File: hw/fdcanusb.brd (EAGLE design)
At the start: 45 x 32 mm, 37 parts, among them J3 JST-ZH6SMT_VERT, M1 MOUNT, M2 MOUNT, M3 MOUNT, M4 MOUNT, U1 MF-REG-SOT235-3.3V-300mA, U2 USBLC6-2SC6, U3 TCAN334GSOT23, U4 TLP3317, U5 STM32G474CEU6

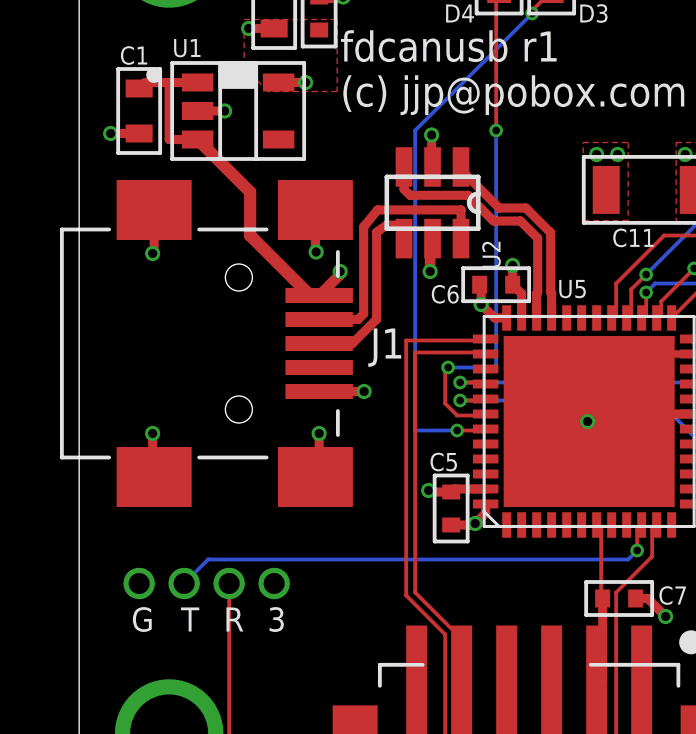
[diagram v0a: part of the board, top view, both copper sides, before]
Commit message: Switch to actually using a micro USB connector
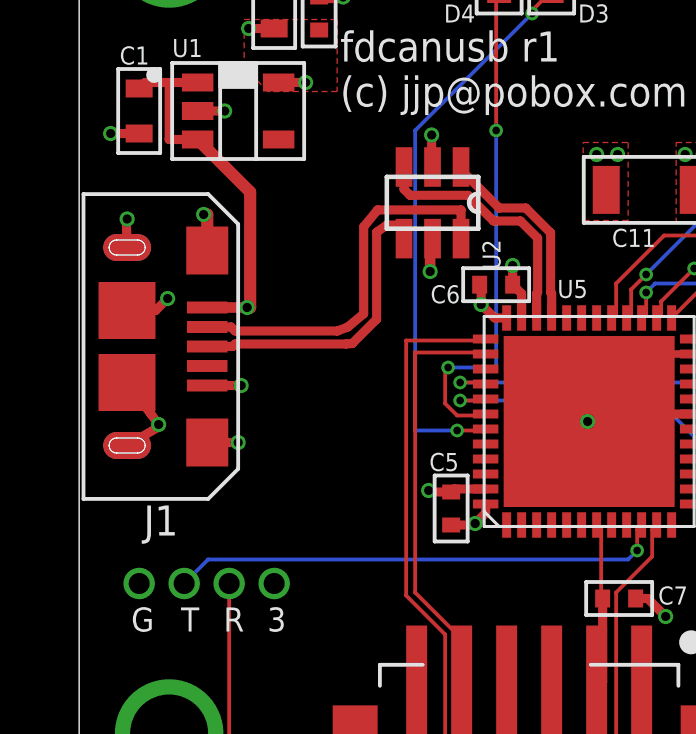
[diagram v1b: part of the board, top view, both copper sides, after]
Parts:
- J1: value (none) -> MF-CON-MICROUSB-RIGHT; device mfconnectors:MINIUSB-RIGHT -> mfconnectors:MICROUSB-RIGHT
- moved J1 5.00 mm to (3.00, 15.9)
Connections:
- net GND: now also J1.S5, J1.S6
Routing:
- net USB_D_N: track 8.93 -> 12.8 mm
- net USB_D_P: track 6.59 -> 10.4 mm
- net VBUS: track 17.2 -> 20.0 mm
- net GND: track 35.9 -> 37.6 mm, vias 25 -> 26
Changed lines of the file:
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@@
 <attribute name="POPULATE" value="0" x="3" y="29" size="1.778" layer="27" display="off"/>
 </element>
-<element name="J1" library="mfconnectors" package="MINIUSB-RIGHT" value="" x="8" y="16" smashed="yes" rot="R270">
-<attribute name="MPN" value="MF-CON-MICROUSB-RIGHT" x="-26.29" y="-20.83" size="1.778" layer="27" rot="R270" display="off"/>
-<attribute name="POPULATE" value="1" x="-26.29" y="-20.83" size="1.778" layer="27" rot="R270" display="off"/>
-<attribute name="HUOSEPART" value="YES" x="-26.29" y="-20.83" size="1.778" layer="27" rot="R270" display="off"/>
-<attribute name="URL" value="http://www.4uconnector.com/online/object/4udrawing/20236.pdf" x="-26.29" y="-20.83" size="1.778" layer="27" rot="R270" display="off"/>
-<attribute name="NAME" x="9.7" y="15.5" size="1" layer="25" font="vector" ratio="10"/>
+<element name="J1" library="mfconnectors" package="MICROUSB-RIGHT" value="MF-CON-MICROUSB-RIGHT" x="3" y="15.9" smashed="yes" rot="R270">
+<attribute name="MPN" value="MF-CON-MICROUSB-RIGHT" x="-31.29" y="-20.93" size="1.778" layer="27" rot="R270" display="off"/>
+<attribute name="POPULATE" value="1" x="-31.29" y="-20.93" size="1.778" layer="27" rot="R270" display="off"/>
+<attribute name="URL" value="https://factory.macrofab.com/part/MF-CON-MICROUSB-RIGHT" x="-31.29" y="-20.93" size="1.778" layer="27" rot="R270" display="off"/>
+<attribute name="NAME" x="3.3" y="10.6" size="1" layer="25" font="vector" ratio="10" rot="R180"/>
+<attribute name="HOUSEPART" value="YES" x="3" y="15.9" size="1.778" layer="27" rot="R270" display="off"/>
+<attribute name="VALUE" value="MF-CON-MICROUSB-RIGHT" x="3" y="15.9" size="1.778" layer="27" rot="R270" display="off"/>
 </element>
 <element name="U1" library="mficpower" package="SOT-23-5" value="MF-REG-SOT235-3.3V-300mA" x="5.3" y="23.75" smashed="yes">
@@
 <via x="11.65" y="11.1" extent="1-16" drill="0.3048"/>
 <via x="14.45" y="18.6" extent="1-16" drill="0.3048"/>
-<via x="2.45" y="13" extent="1-16" drill="0.3048"/>
-<via x="2.45" y="19" extent="1-16" drill="0.3048"/>
-<via x="7.9" y="19.05" extent="1-16" drill="0.3048"/>
-<via x="8" y="13" extent="1-16" drill="0.3048"/>
+<via x="2.65" y="13.3" extent="1-16" drill="0.3048"/>
+<via x="2.95" y="17.5" extent="1-16" drill="0.3048"/>
+<via x="1.6" y="20.15" extent="1-16" drill="0.3048"/>
+<via x="5.3" y="12.7" extent="1-16" drill="0.3048"/>
 <via x="11.75" y="22.95" extent="1-16" drill="0.3048"/>
-<via x="9.5" y="14.4" extent="1-16" drill="0.3048"/>
-<wire x1="8" y1="14.4" x2="9.5" y2="14.4" width="0.3048" layer="1"/>
-<wire x1="8" y1="13" x2="8" y2="11.675" width="0.3048" layer="1"/>
-<wire x1="8" y1="11.675" x2="7.875" y2="11.55" width="0.3048" layer="1"/>
-<wire x1="2.45" y1="13" x2="2.45" y2="11.6" width="0.3048" layer="1"/>
-<wire x1="2.45" y1="11.6" x2="2.5" y2="11.55" width="0.3048" layer="1"/>
-<wire x1="2.5" y1="20.45" x2="2.5" y2="19.05" width="0.3048" layer="1"/>
-<wire x1="2.5" y1="19.05" x2="2.45" y2="19" width="0.3048" layer="1"/>
-<wire x1="7.875" y1="20.45" x2="7.875" y2="19.075" width="0.3048" layer="1"/>
-<wire x1="7.875" y1="19.075" x2="7.9" y2="19.05" width="0.3048" layer="1"/>
+<via x="5.4" y="14.6" extent="1-16" drill="0.3048"/>
+<wire x1="4.27" y1="14.6" x2="5.4" y2="14.6" width="0.3048" layer="1"/>
+<wire x1="1.6" y1="19.2" x2="1.575" y2="19.975" width="0.3048" layer="1"/>
+<wire x1="1.575" y1="19.975" x2="1.6" y2="20.15" width="0.3048" layer="1"/>
 <wire x1="2" y1="23" x2="1.05" y2="23" width="0.3048" layer="1"/>
 <wire x1="3.95" y1="23.75" x2="4.85" y2="23.75" width="0.3048" layer="1"/>
@@
 <wire x1="19.25" y1="15.65" x2="17" y2="13.4" width="0.254" layer="1" curve="90"/>
 <wire x1="17" y1="13.4" x2="16.95" y2="13.4" width="0.127" layer="1"/>
+<contactref element="J1" pad="S5"/>
+<contactref element="J1" pad="S6"/>
+<via x="4.15" y="20.3" extent="1-16" drill="0.3048"/>
+<wire x1="2.95" y1="17.5" x2="2.55" y2="17.1" width="0.3048" layer="1"/>
+<wire x1="2.55" y1="17.1" x2="1.595" y2="17.1" width="0.3048" layer="1"/>
+<wire x1="2.65" y1="13.3" x2="2.7" y2="13.25" width="0.3048" layer="1"/>
+<wire x1="2.7" y1="13.25" x2="1.6" y2="12.6" width="0.3048" layer="1"/>
+<wire x1="2.65" y1="13.3" x2="2.395" y2="13.645" width="0.3048" layer="1"/>
+<wire x1="2.395" y1="13.645" x2="1.595" y2="14.7" width="0.3048" layer="1"/>
+<wire x1="5.3" y1="12.7" x2="4.27" y2="12.7" width="0.3048" layer="1"/>
+<wire x1="4.27" y1="19.1" x2="4.27" y2="20.3" width="0.4064" layer="1"/>
+<wire x1="4.27" y1="20.3" x2="4.15" y2="20.3" width="0.4064" layer="1"/>
 </signal>
 <signal name="VBUS">
@@
 <wire x1="3.95" y1="22.8" x2="3" y2="22.8" width="0.3048" layer="1"/>
 <wire x1="3" y1="22.8" x2="3" y2="24.7" width="0.3048" layer="1"/>
-<wire x1="8" y1="17.6" x2="7.7" y2="17.6" width="0.4064" layer="1"/>
-<wire x1="7.7" y1="17.6" x2="5.7" y2="19.6" width="0.4064" layer="1"/>
-<wire x1="5.7" y1="19.6" x2="5.7" y2="21.05" width="0.4064" layer="1"/>
 <wire x1="5.7" y1="21.05" x2="3.95" y2="22.8" width="0.4064" layer="1"/>
-<via x="8.7" y="18.4" extent="1-16" drill="0.3048"/>
+<via x="5.6" y="17.2" extent="1-16" drill="0.3048"/>
 <via x="11.7" y="18.4" extent="1-16" drill="0.3048"/>
-<wire x1="8.7" y1="18.4" x2="11.7" y2="18.4" width="0.3556" layer="2"/>
-<wire x1="8" y1="17.6" x2="8.7" y2="18.3" width="0.3556" layer="1"/>
-<wire x1="8.7" y1="18.3" x2="8.7" y2="18.4" width="0.3556" layer="1"/>
+<wire x1="5.6" y1="17.2" x2="11.7" y2="18.4" width="0.3556" layer="2"/>
+<wire x1="4.27" y1="17.2" x2="5.6" y2="17.2" width="0.3556" layer="1"/>
 <wire x1="11.78" y1="19.4962" x2="11.7" y2="19.4162" width="0.3556" layer="1"/>
 <wire x1="11.7" y1="19.4162" x2="11.7" y2="18.4" width="0.3556" layer="1"/>
+<wire x1="5.7" y1="21.05" x2="5.7" y2="17.2" width="0.4064" layer="1"/>
+<wire x1="5.7" y1="17.2" x2="5.6" y2="17.2" width="0.4064" layer="1"/>
 </signal>
 <signal name="USB_D_N" class="1">
 <contactref element="J1" pad="2"/>
 <contactref element="U2" pad="6"/>
-<wire x1="8" y1="16.8" x2="9.29466875" y2="16.8" width="0.3048" layer="1"/>
-<wire x1="9.29466875" y1="16.8" x2="9.4841" y2="16.98943125" width="0.3048" layer="1"/>
+<wire x1="8.95466875" y1="16.55" x2="9.4841" y2="16.98943125" width="0.3048" layer="1"/>
 <wire x1="9.4841" y1="16.98943125" x2="9.4841" y2="19.88943125" width="0.3048" layer="1"/>
 <wire x1="9.4841" y1="19.88943125" x2="9.947334375" y2="20.452665625" width="0.3048" layer="1"/>
 <wire x1="9.947334375" y1="20.452665625" x2="12.73" y2="20.452665625" width="0.3048" layer="1"/>
 <wire x1="12.73" y1="20.452665625" x2="12.73" y2="19.4962" width="0.3048" layer="1"/>
+<wire x1="8.95466875" y1="16.55" x2="8.60466875" y2="16.4159" width="0.3048" layer="1"/>
+<wire x1="8.60466875" y1="16.4159" x2="5.2" y2="16.4159" width="0.3048" layer="1"/>
+<wire x1="5.2" y1="16.4159" x2="5.0659" y2="16.55" width="0.3048" layer="1"/>
+<wire x1="5.0659" y1="16.55" x2="4.27" y2="16.55" width="0.3048" layer="1"/>
 </signal>
 <signal name="USB_D_P" class="1">
 <contactref element="J1" pad="3"/>
 <contactref element="U2" pad="4"/>
-<wire x1="8" y1="16" x2="9.10533125" y2="16" width="0.3048" layer="1"/>
 <wire x1="9.10533125" y1="16" x2="9.9159" y2="16.81056875" width="0.3048" layer="1"/>
 <wire x1="9.9159" y1="16.81056875" x2="9.9159" y2="19.71056875" width="0.3048" layer="1"/>
@@
 <wire x1="10.252665625" y1="19.947334375" x2="10.83" y2="19.947334375" width="0.3048" layer="1"/>
 <wire x1="10.83" y1="19.947334375" x2="10.83" y2="19.4962" width="0.3048" layer="1"/>
+<wire x1="9.10533125" y1="16" x2="8.90533125" y2="15.9841" width="0.3048" layer="1"/>
+<wire x1="8.90533125" y1="15.9841" x2="5.2" y2="15.9841" width="0.3048" layer="1"/>
+<wire x1="5.2" y1="15.9841" x2="5.1159" y2="15.9" width="0.3048" layer="1"/>
+<wire x1="5.1159" y1="15.9" x2="4.27" y2="15.9" width="0.3048" layer="1"/>
 </signal>
 <signal name="USB_F_N" class="1">

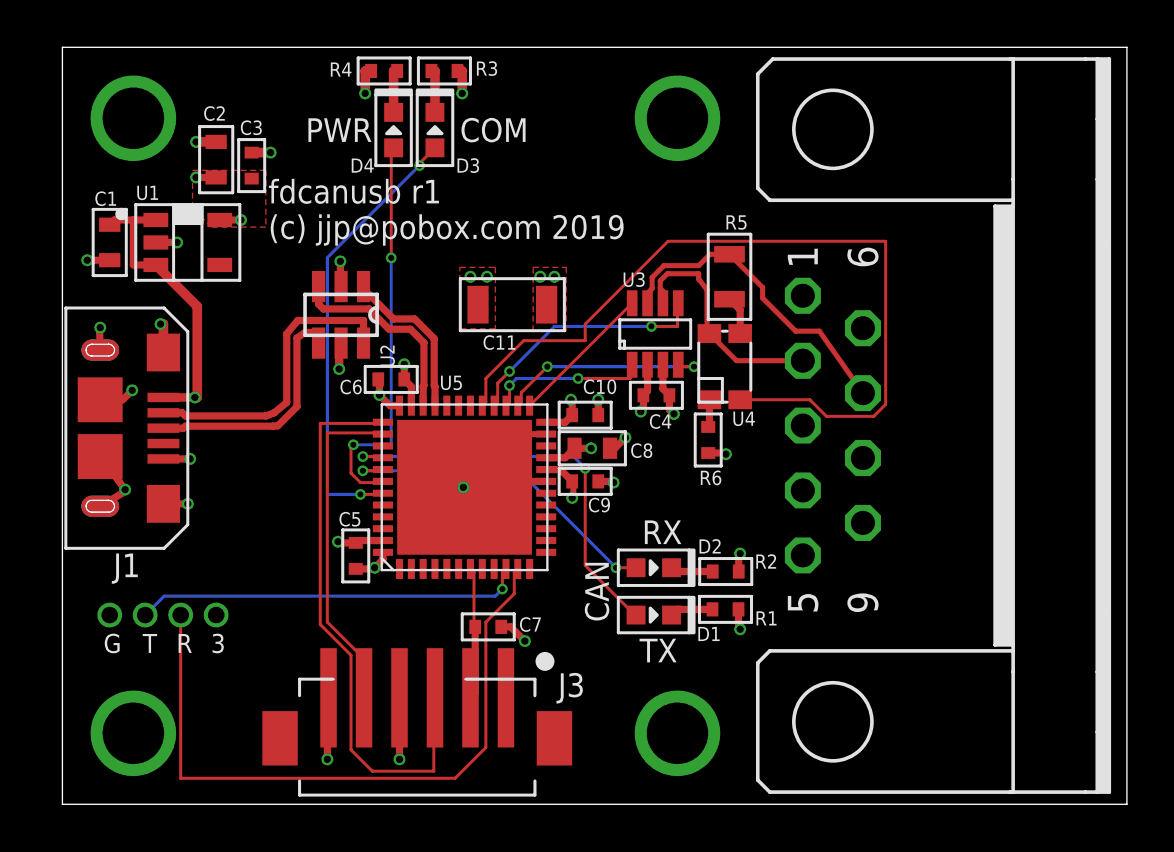
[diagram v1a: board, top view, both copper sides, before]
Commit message: Update to use correct STM32 pinout
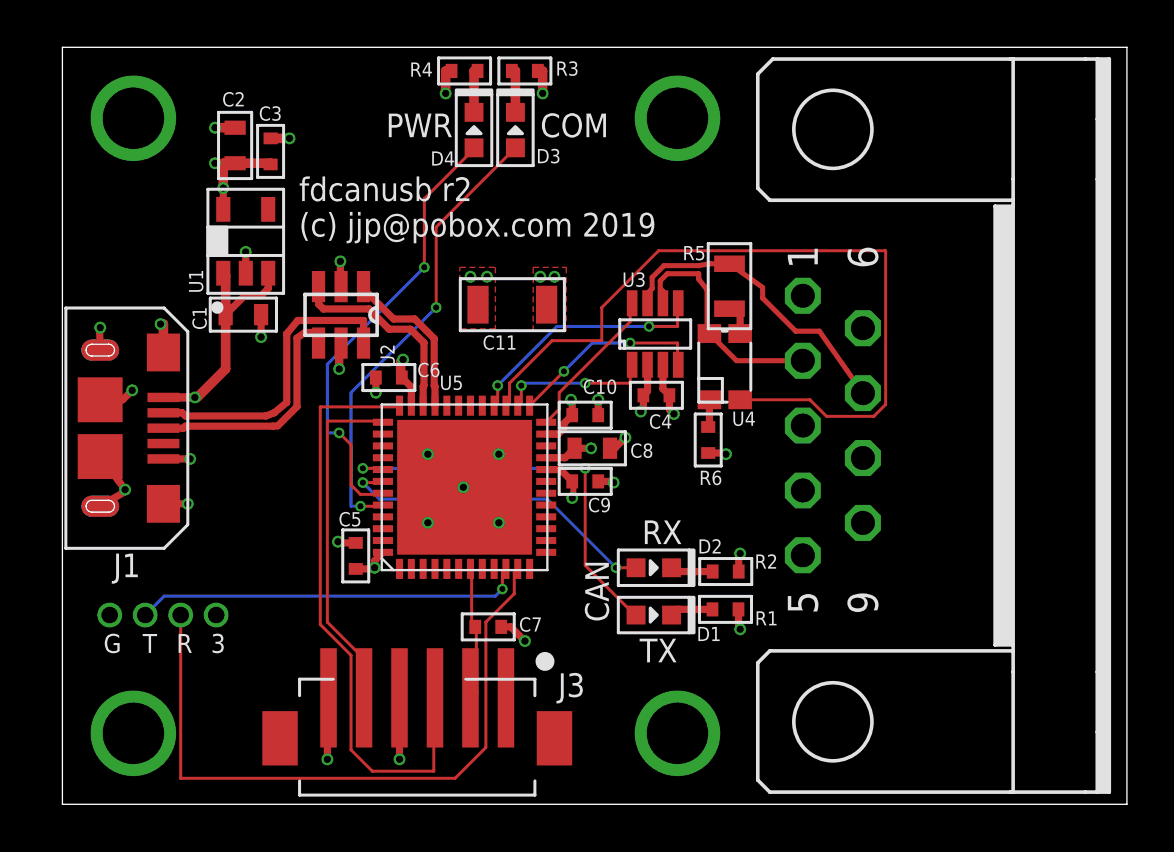
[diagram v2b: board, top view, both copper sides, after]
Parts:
- R1, R2, R3, R4: value 220 -> 560
- moved C1 6.42 mm to (7.65, 20.7), turned to 0 degrees
- moved R3 3.40 mm to (19.6, 31.0)
- moved R4 3.40 mm to (17.0, 31.0)
- moved D3 3.40 mm to (19.1, 28.5)
- moved D4 3.40 mm to (17.4, 28.5)
- moved U1 2.45 mm to (7.75, 23.8), turned to 90 degrees
- moved C3 1.00 mm to (8.80, 27.6)
- moved C2 1.00 mm to (7.30, 27.9)
- moved R5 0.40 mm to (28.2, 21.9)
- moved C6 0.13 mm to (13.8, 18.0), turned to 180 degrees
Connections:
- net +3V3: now also U5.23, U5.35; no longer U5.24, U5.36
- net CAN_RX: now also U5.25; no longer U5.26
- net CAN_STB: now also U5.24; no longer U5.25
- net CAN_TERM: now also U5.27; no longer U5.29
- net CAN_TX: now also U5.26; no longer U5.27
- net GND: no longer U5.19, U5.23, U5.35, U5.47
- net LED_CAN_RX: now also U5.42; no longer U5.41
- net LED_CAN_TX: now also U5.41; no longer U5.40
- net LED_COM: now also U5.44; no longer U5.43
- net LED_PWR: now also U5.43; no longer U5.42
- net SWCLK: now also U5.37; no longer U5.38
- net SWDIO: now also U5.36; no longer U5.37
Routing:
- net GND: track 37.6 -> 30.9 mm, vias 26 -> 30
- net +3V3: track 17.5 -> 20.8 mm
- net VBUS: track 20.0 -> 17.5 mm
- net LED_PWR: track 17.0 -> 19.1 mm
- net SWDIO: track 24.0 -> 25.4 mm
- net CAN_TERM: track 34.5 -> 33.2 mm
- net CAN_RX: track 9.07 -> 8.29 mm
- net SWCLK: track 14.2 -> 14.7 mm
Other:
- board text added: "fdcanusb r2 (c) jjp@pobox.com 2019"
- board text removed: "fdcanusb r1 (c) jjp@pobox.com 2019"
